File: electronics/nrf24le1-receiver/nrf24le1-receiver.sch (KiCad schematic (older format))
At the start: 16 parts, among them K1 CONN_3, K2 CONN_3, K3 CONN_3, K4 CONN_3, SW1 SW_PUSH, U1 MCP1703T-3302E/CB, U2 NRF24LE1-MODULE-15X21

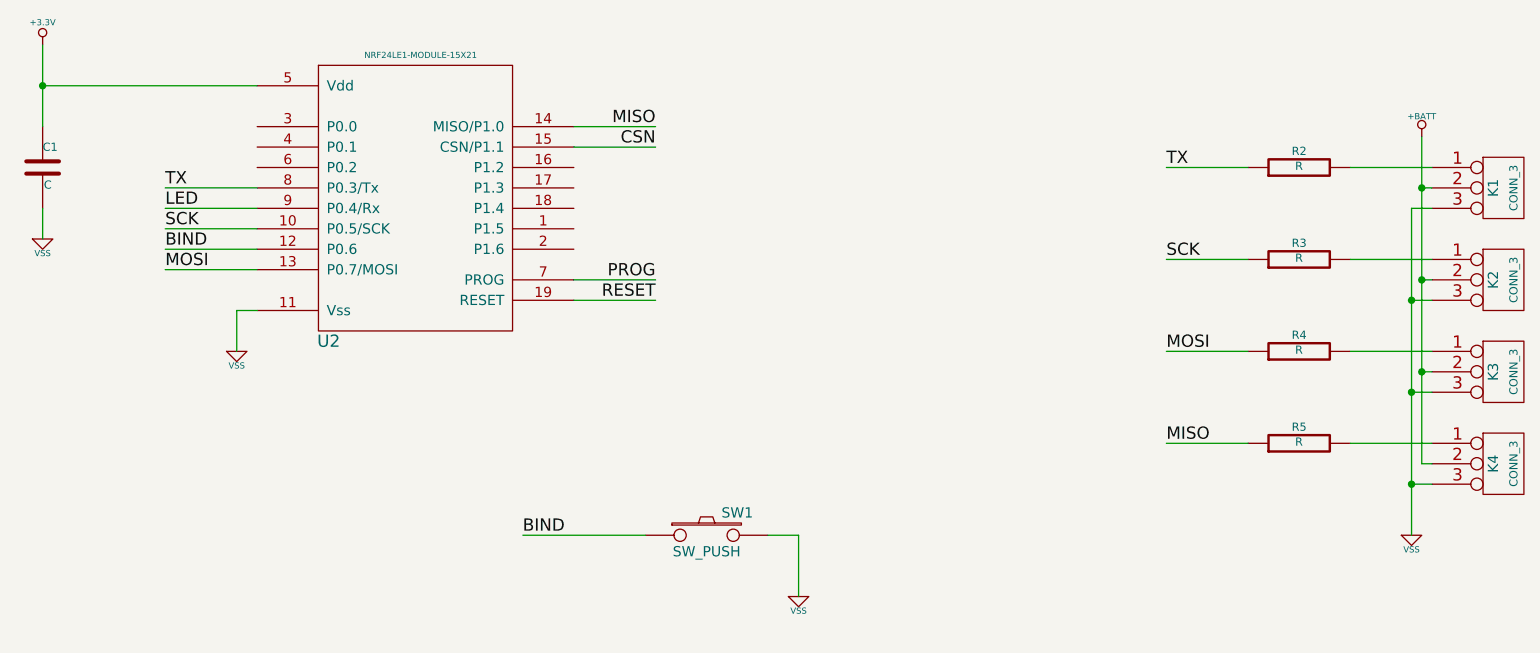
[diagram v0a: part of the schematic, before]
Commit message: Tweak schematics and layout
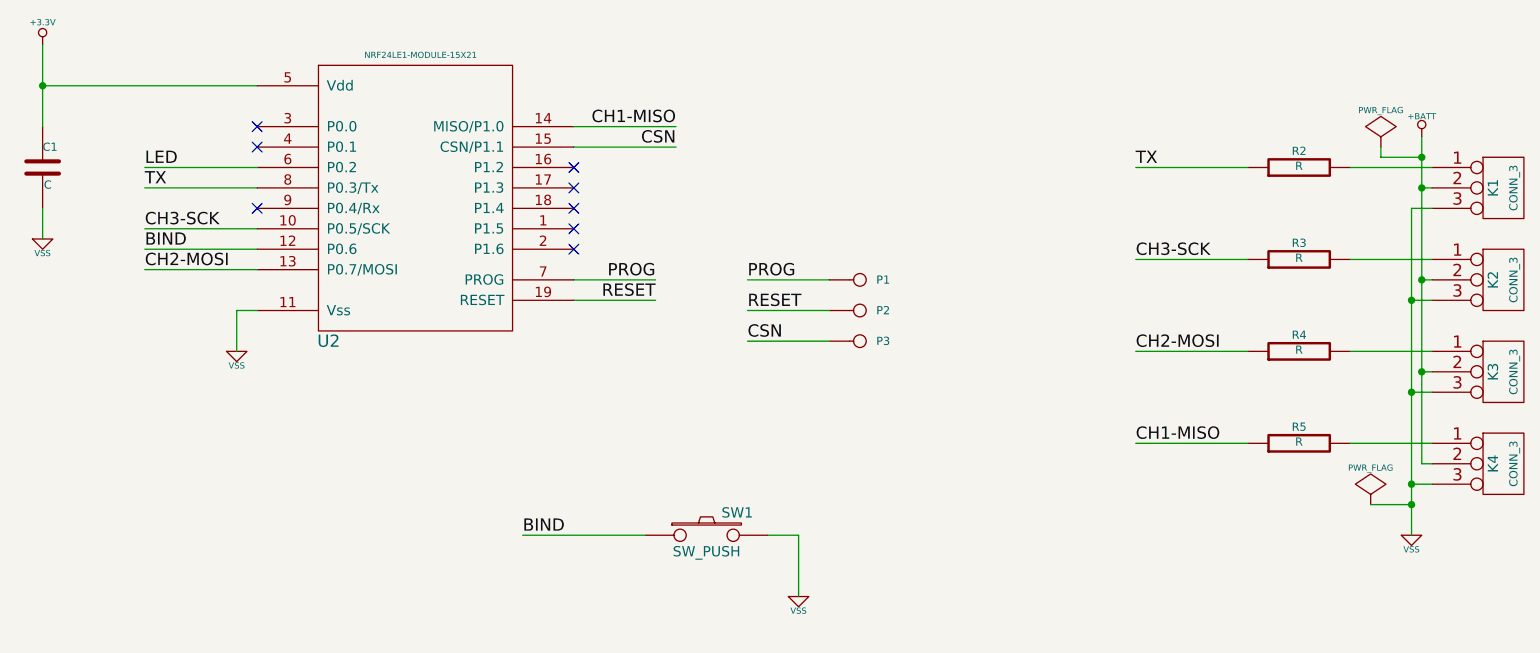
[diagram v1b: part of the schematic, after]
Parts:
- added P1, P2, P3: CONN_1, symbol CONN_1
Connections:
- net CSN: now also P3.1
- net LED: now also U2.6 (P0.2); no longer U2.9 (P0.4/Rx)
- net PROG: now also P1.1
- net RESET: now also P2.1
- net MISO renamed CH1-MISO
- net MOSI renamed CH2-MOSI
- net SCK renamed CH3-SCK
- no-connect marks 0 -> 8

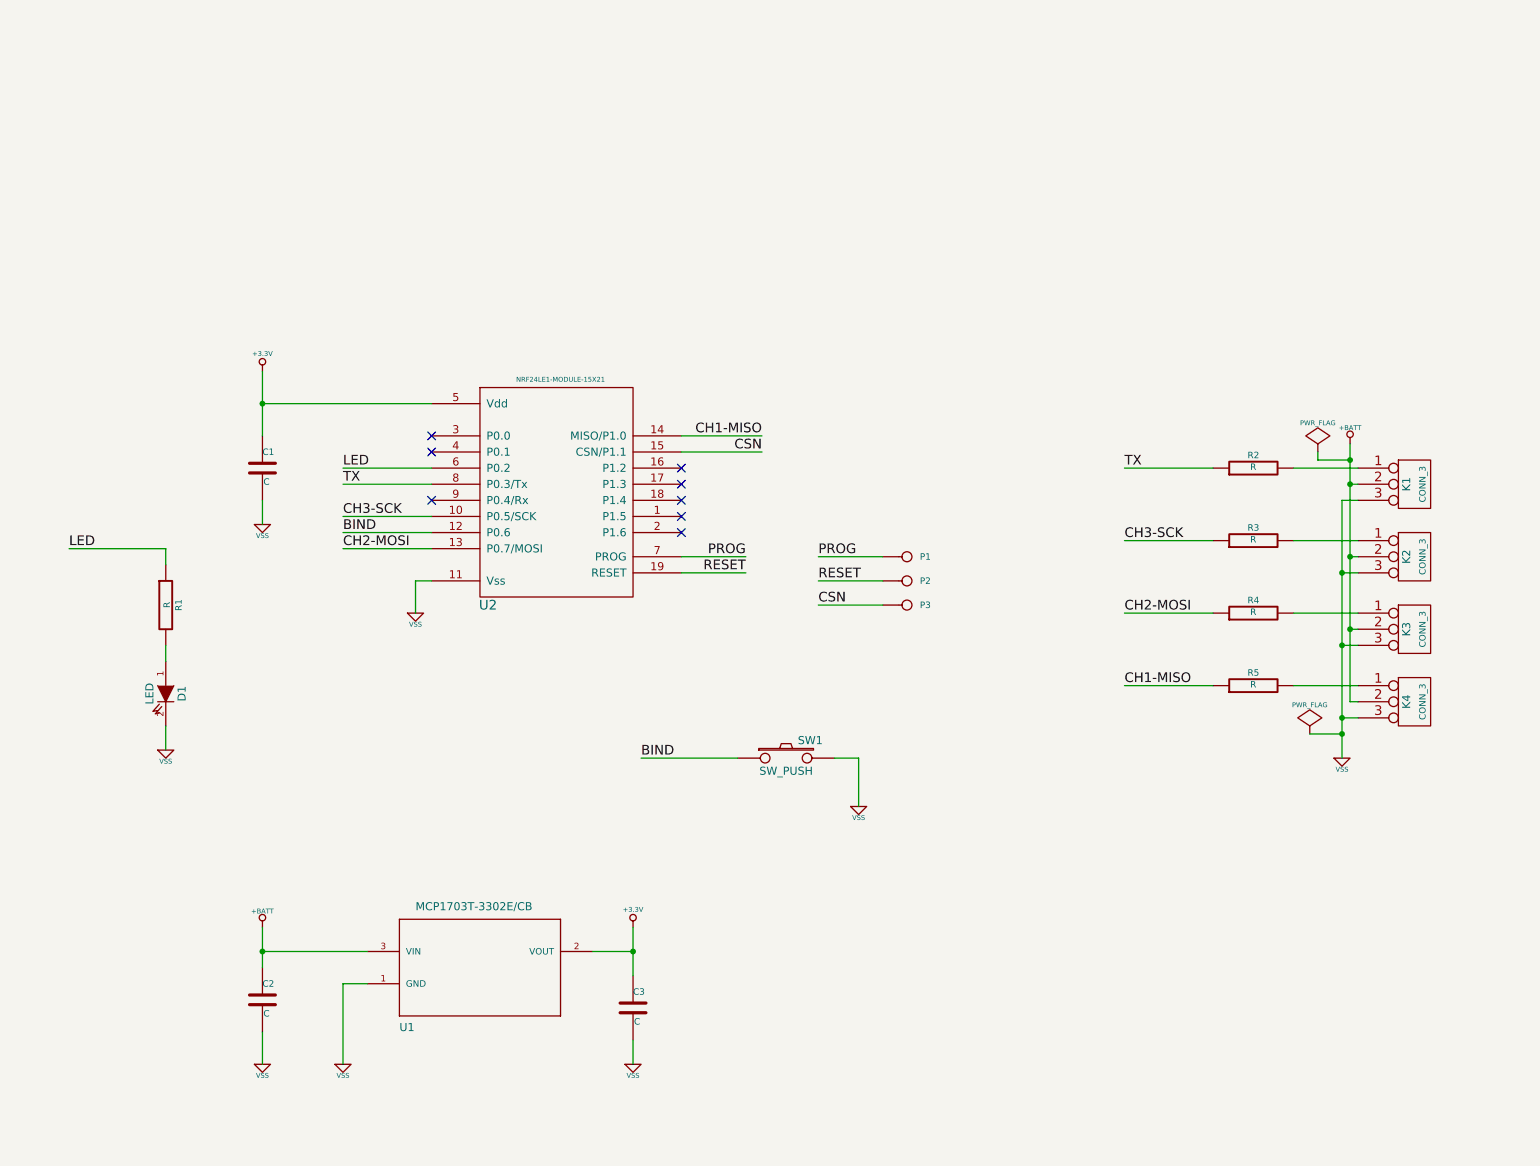
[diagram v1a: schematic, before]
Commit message: Improve silk screen
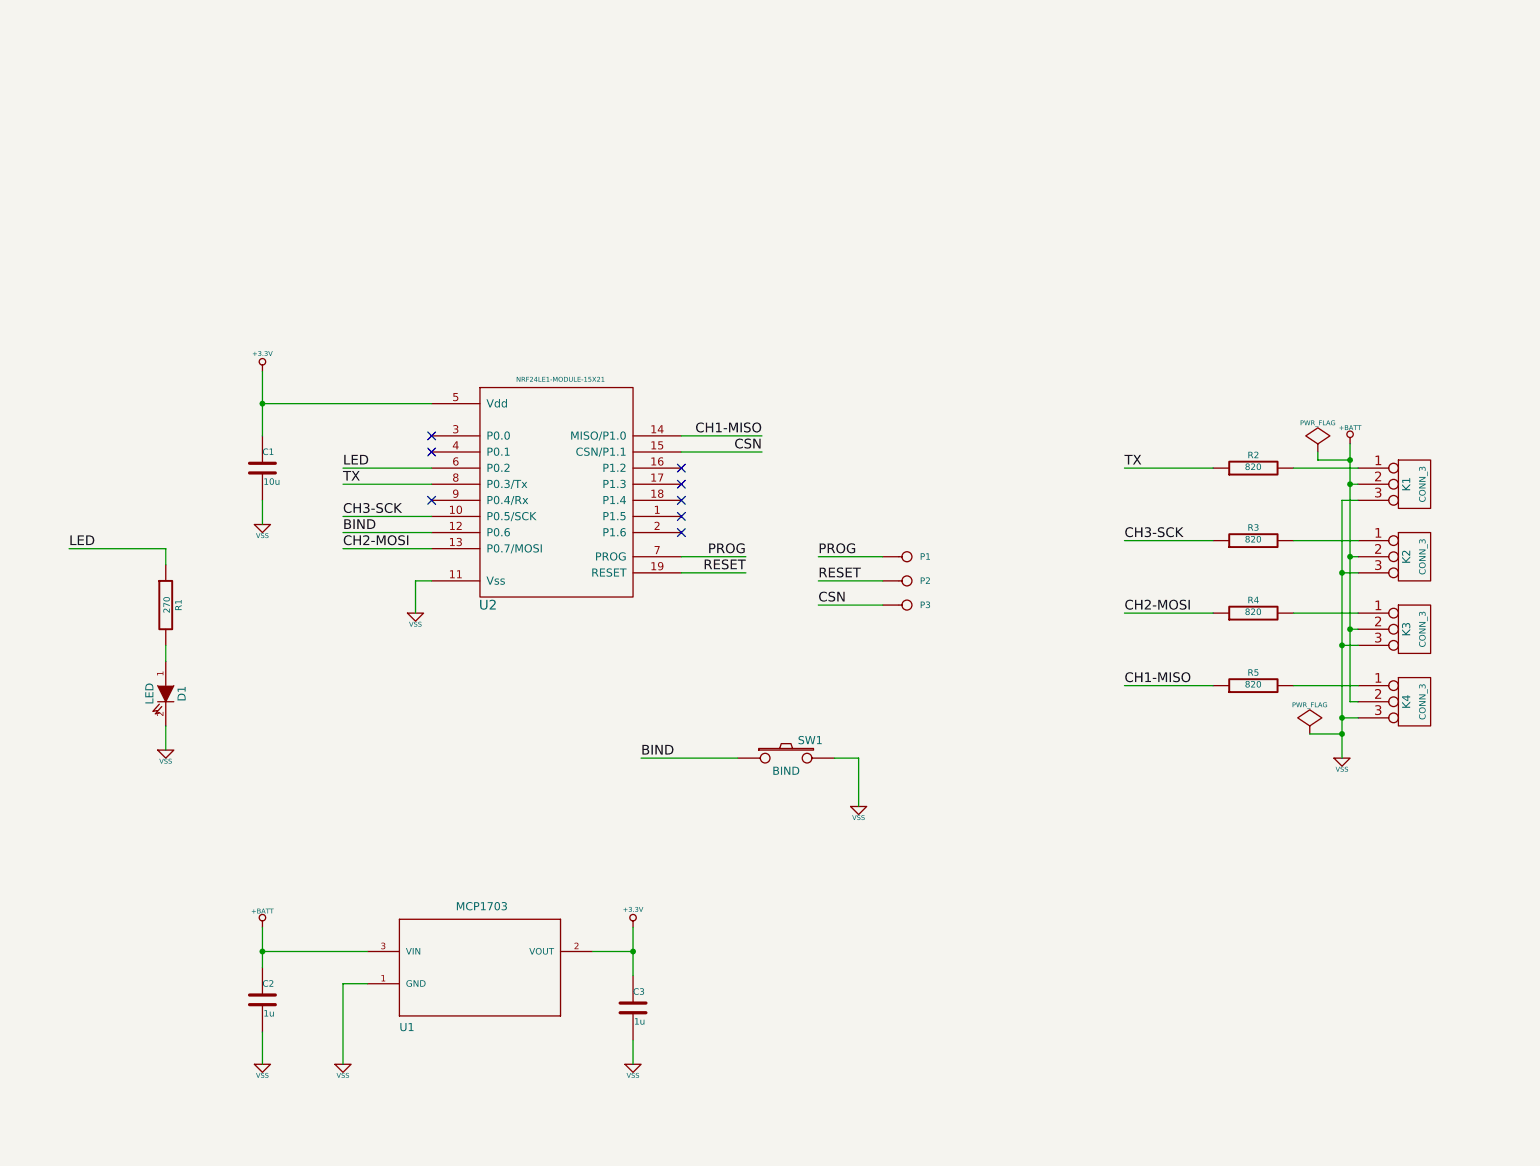
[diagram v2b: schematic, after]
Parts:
- C1: value C -> 10u
- C2, C3: value C -> 1u
- R1: value R -> 270
- R2, R3, R4, R5: value R -> 820
- SW1: value SW_PUSH -> BIND
- U1: value MCP1703T-3302E/CB -> MCP1703
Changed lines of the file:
@@
 P 3650 5600
 F 0 "U1" H 3150 5100 50  0000 L BNN
-F 1 "MCP1703T-3302E/CB" H 3250 5850 50  0000 L BNN
+F 1 "MCP1703" H 3500 5850 50  0000 L BNN
 F 2 "MCP1703-SOT95P300X145-3N" H 3800 5150 30  0001 C CNN
 F 3 "~" H 3650 5600 60  0000 C CNN
@@
 P 4600 5950
 F 0 "C3" H 4600 6050 40  0000 L CNN
-F 1 "C" H 4606 5865 40  0000 L CNN
+F 1 "1u" H 4606 5865 40  0000 L CNN
 F 2 "~" H 4638 5800 30  0000 C CNN
 F 3 "~" H 4600 5950 60  0000 C CNN
@@
 P 2300 5900
 F 0 "C2" H 2300 6000 40  0000 L CNN
-F 1 "C" H 2306 5815 40  0000 L CNN
+F 1 "1u" H 2306 5815 40  0000 L CNN
 F 2 "~" H 2338 5750 30  0000 C CNN
 F 3 "~" H 2300 5900 60  0000 C CNN
@@
 P 2300 2600
 F 0 "C1" H 2300 2700 40  0000 L CNN
-F 1 "C" H 2306 2515 40  0000 L CNN
+F 1 "10u" H 2306 2515 40  0000 L CNN
 F 2 "~" H 2338 2450 30  0000 C CNN
 F 3 "~" H 2300 2600 60  0000 C CNN
@@
 P 8450 2600
 F 0 "R2" V 8530 2600 40  0000 C CNN
-F 1 "R" V 8457 2601 40  0000 C CNN
+F 1 "820" V 8457 2601 40  0000 C CNN
 F 2 "~" V 8380 2600 30  0000 C CNN
 F 3 "~" H 8450 2600 30  0000 C CNN
@@
 P 8450 3050
 F 0 "R3" V 8530 3050 40  0000 C CNN
-F 1 "R" V 8457 3051 40  0000 C CNN
+F 1 "820" V 8457 3051 40  0000 C CNN
 F 2 "~" V 8380 3050 30  0000 C CNN
 F 3 "~" H 8450 3050 30  0000 C CNN
@@
 P 8450 3500
 F 0 "R4" V 8530 3500 40  0000 C CNN
-F 1 "R" V 8457 3501 40  0000 C CNN
+F 1 "820" V 8457 3501 40  0000 C CNN
 F 2 "~" V 8380 3500 30  0000 C CNN
 F 3 "~" H 8450 3500 30  0000 C CNN
@@
 P 8450 3950
 F 0 "R5" V 8530 3950 40  0000 C CNN
-F 1 "R" V 8457 3951 40  0000 C CNN
+F 1 "820" V 8457 3951 40  0000 C CNN
 F 2 "~" V 8380 3950 30  0000 C CNN
 F 3 "~" H 8450 3950 30  0000 C CNN
@@
 P 5550 4400
 F 0 "SW1" H 5700 4510 50  0000 C CNN
-F 1 "SW_PUSH" H 5550 4320 50  0000 C CNN
+F 1 "BIND" H 5550 4320 50  0000 C CNN
 F 2 "~" H 5550 4400 60  0000 C CNN
 F 3 "~" H 5550 4400 60  0000 C CNN
@@
 P 1700 3450
 F 0 "R1" V 1780 3450 40  0000 C CNN
-F 1 "R" V 1707 3451 40  0000 C CNN
+F 1 "270" V 1707 3451 40  0000 C CNN
 F 2 "~" V 1630 3450 30  0000 C CNN
 F 3 "~" H 1700 3450 30  0000 C CNN

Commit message: Make pinout similar to XR3100
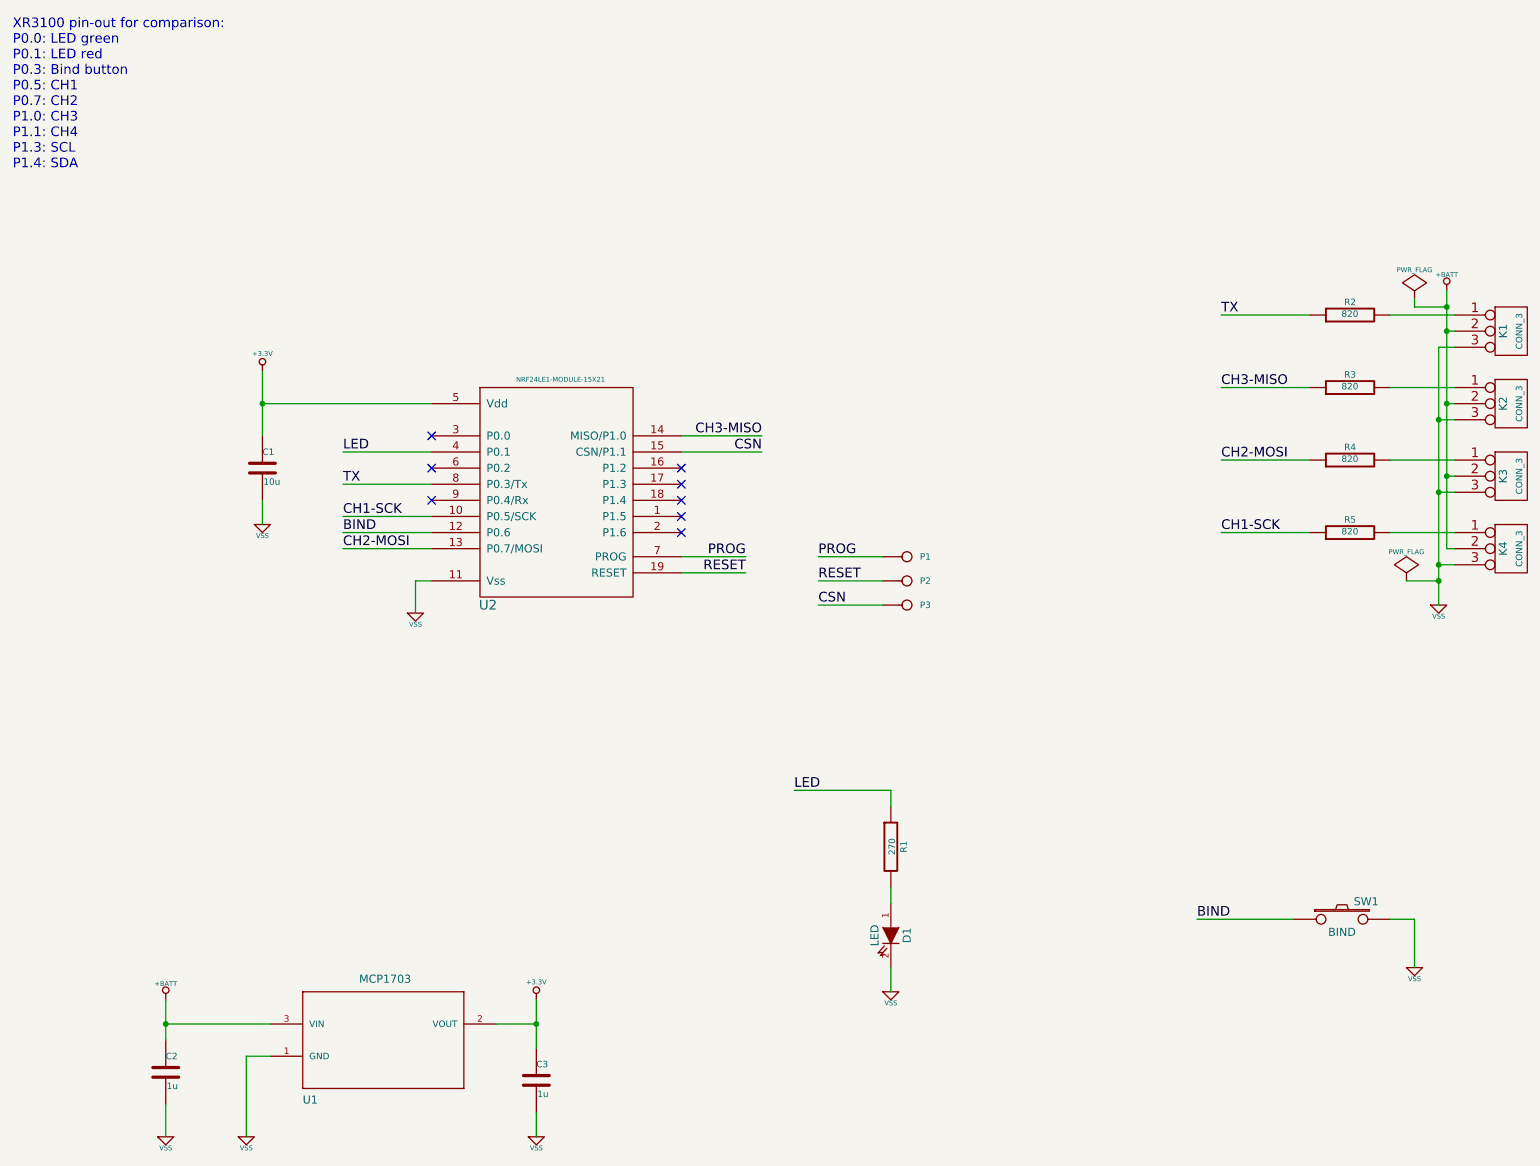
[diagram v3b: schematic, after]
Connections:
- net LED: now also U2.4 (P0.1); no longer U2.6 (P0.2)
- net CH1-MISO renamed CH1-SCK
- net CH1-SCK: now also U2.10 (P0.5/SCK); no longer U2.14 (MISO/P1.0)
- net CH3-SCK renamed CH3-MISO
- net CH3-MISO: now also U2.14 (MISO/P1.0); no longer U2.10 (P0.5/SCK)
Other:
- note added: "XR3100 pin-out for comparison:\nP0.0: LED green\nP0.1: LED red\nP0.3: Bind button\nP0.5: CH1\nP0.7: CH2\nP1.0: CH3\nP1.1: CH4\nP1.3: SCL\nP1.4: SDA"
- moved on the sheet: C2, C3, D1, K1, K2, K3, K4, R1, R2, R3, R4, R5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
